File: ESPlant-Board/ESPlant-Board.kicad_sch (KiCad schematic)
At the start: 36 parts, among them J1 Conn_01x05, U13 ESP32-C6-MINI-1/U, U3 Reset, U4 Boot, U5 Temp/Humid-Sensor, U6 Light sensor, U7 AMS1117-3_3, U8 MK-12C02-G025

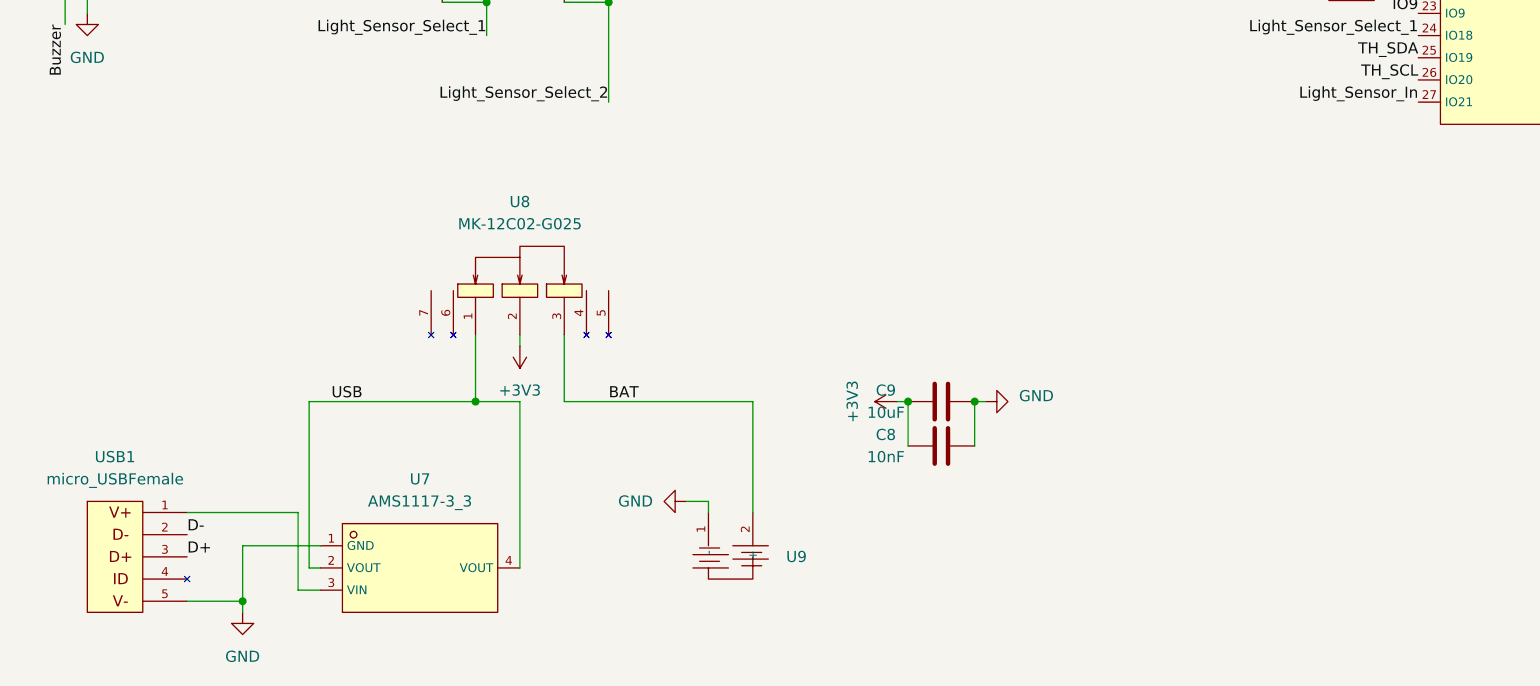
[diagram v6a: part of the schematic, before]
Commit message: Board: Replace Micro USB with USB type c
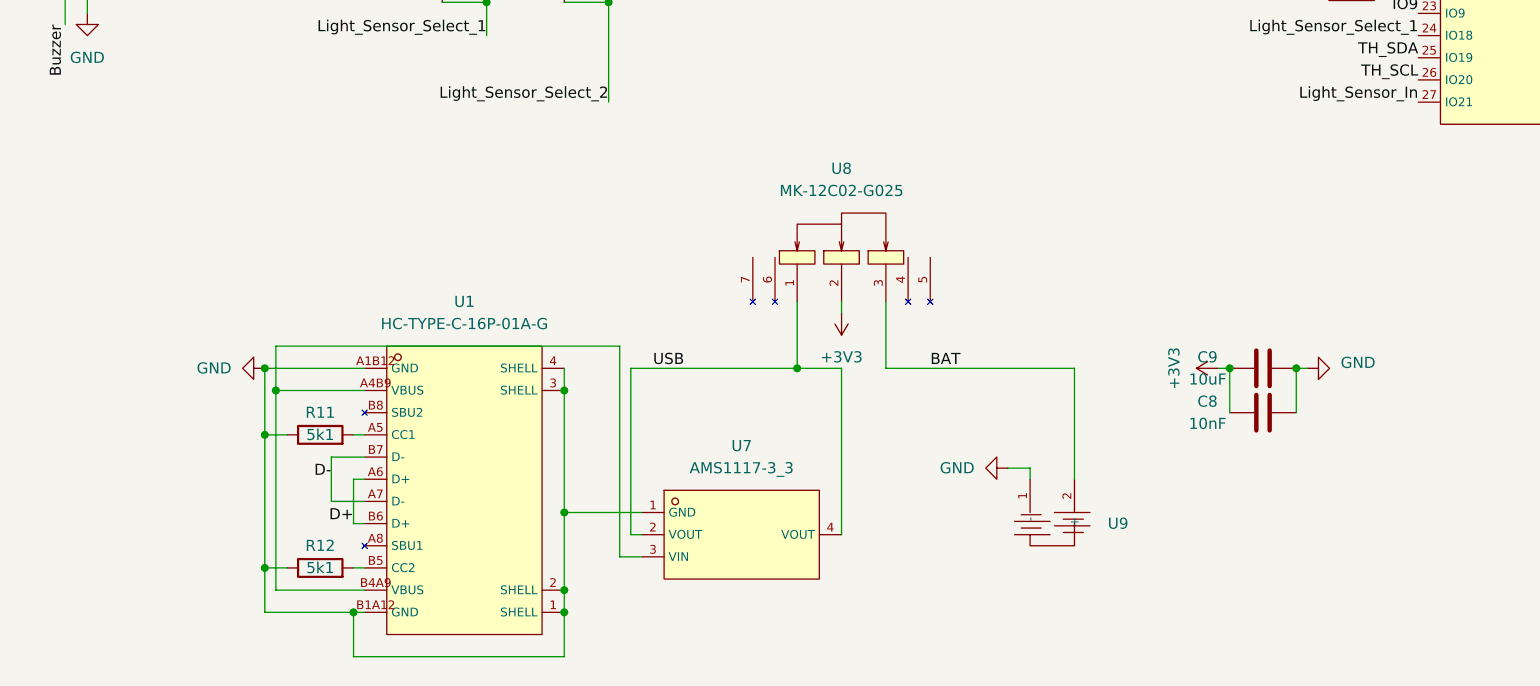
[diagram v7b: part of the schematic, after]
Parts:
- removed USB1: micro_USBFemale, CustomFootprints:MICRO-USB-SMD_5P-P0.65-H-F_C10418, symbol Custom_Parts:micro_USBFemale
- added R11, R12: 5k1, Resistor_SMD:R_0402_1005Metric, symbol Device:R
- added U1: HC-TYPE-C-16P-01A-G, CustomFootprints:USB-C-SMD_G-SWITCH_GT-USB-7010EN, symbol Custom_Parts:HC-TYPE-C-16P-01A-G
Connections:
- net D+: now also U1.A6 (D+), U1.B6 (D+)
- net D-: now also U1.A7 (D-), U1.B7 (D-)
- net GND: now also R11.1, R12.1, U1.1 (SHELL), U1.2 (SHELL), U1.3 (SHELL), U1.4 (SHELL), U1.A1B12 (GND), U1.B1A12 (GND)
- net at U7.3 (VIN): now also U1.A4B9 (VBUS), U1.B4A9 (VBUS)
- new net: R12.2, U1.B5 (CC2)
- new net: R11.2, U1.A5 (CC1)
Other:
- moved on the sheet: C8, C9, U7, U8, U9

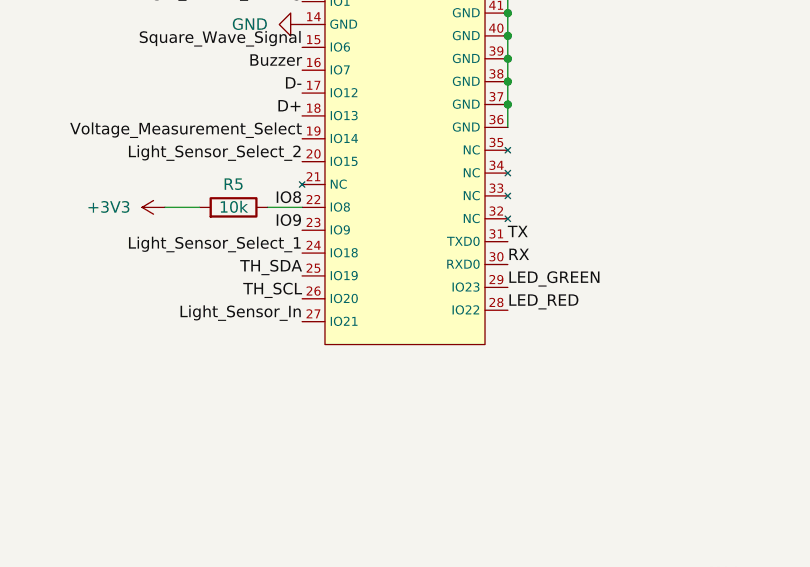
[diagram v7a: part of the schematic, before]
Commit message: Board: Make board smaller
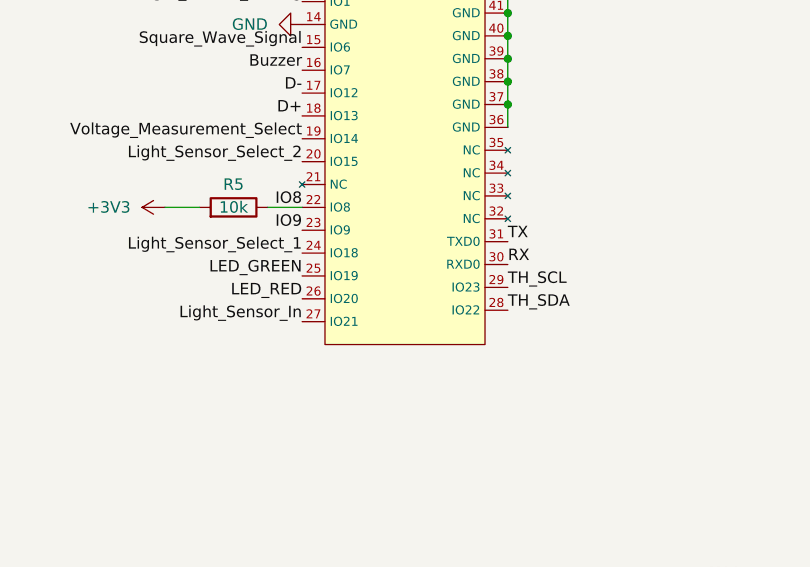
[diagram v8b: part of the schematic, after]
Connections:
- net LED_GREEN: now also U13.25 (IO19); no longer U13.29 (IO23)
- net LED_RED: now also U13.26 (IO20); no longer U13.28 (IO22)
- net TH_SCL: now also U13.29 (IO23); no longer U13.26 (IO20)
- net TH_SDA: now also U13.28 (IO22); no longer U13.25 (IO19)
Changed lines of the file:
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@@
     (effects (font (size 1.27 1.27)) (justify left bottom))
   )
-  (label "LED_RED" (at 195.58 129.54 0) (fields_autoplaced)
-    (effects (font (size 1.27 1.27)) (justify left bottom))
+  (label "LED_RED" (at 172.72 128.27 180) (fields_autoplaced)
+    (effects (font (size 1.27 1.27)) (justify right bottom))
   )
   (label "TH_SCL" (at 20.32 93.98 180) (fields_autoplaced)
@@
     (effects (font (size 1.27 1.27)) (justify right bottom))
   )
-  (label "TH_SCL" (at 172.72 128.27 180) (fields_autoplaced)
-    (effects (font (size 1.27 1.27)) (justify right bottom))
+  (label "TH_SCL" (at 195.58 127 0) (fields_autoplaced)
+    (effects (font (size 1.27 1.27)) (justify left bottom))
   )
   (label "Square_Wave_Signal" (at 172.72 100.33 180) (fields_autoplaced)
@@
     (effects (font (size 1.27 1.27)) (justify left bottom))
   )
-  (label "TH_SDA" (at 172.72 125.73 180) (fields_autoplaced)
-    (effects (font (size 1.27 1.27)) (justify right bottom))
+  (label "TH_SDA" (at 195.58 129.54 0) (fields_autoplaced)
+    (effects (font (size 1.27 1.27)) (justify left bottom))
   )
   (label "Light_Sensor_Select_1" (at 66.04 123.19 180) (fields_autoplaced)
@@
     (effects (font (size 1.27 1.27)) (justify right bottom))
   )
-  (label "LED_GREEN" (at 195.58 127 0) (fields_autoplaced)
-    (effects (font (size 1.27 1.27)) (justify left bottom))
+  (label "LED_GREEN" (at 172.72 125.73 180) (fields_autoplaced)
+    (effects (font (size 1.27 1.27)) (justify right bottom))
   )
   (label "Square_Wave_Signal" (at 78.74 77.47 0) (fields_autoplaced)
